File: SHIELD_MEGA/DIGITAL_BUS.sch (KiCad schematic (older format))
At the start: 38 parts

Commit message: Finished digital sheet
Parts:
- removed J?: Conn_01x03_Male, symbol Connector:Conn_01x03_Male
- added J?: Conn_01x03_Male, symbol Connector:Conn_01x03_Male
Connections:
- net 5V: now also J?.2 (Pin_2)
- net DGND: now also J?.3 (Pin_3)
- net D12: now reaches J?.1 (Pin_1)
- net D13: now reaches J?.1 (Pin_1)
- net D22: now reaches J?.1 (Pin_1)
- net D23: now reaches J?.1 (Pin_1)
- net D24: now reaches J?.1 (Pin_1)
- net D25: now reaches J?.1 (Pin_1)
- net D26: now reaches J?.1 (Pin_1)
- net D28: now reaches J?.1 (Pin_1)
- net D29: now reaches J?.1 (Pin_1)
- net D30: now reaches J?.1 (Pin_1)
- net D31: now reaches J?.1 (Pin_1)
- net D32: now reaches J?.1 (Pin_1)
- net D33: now reaches J?.1 (Pin_1)
- net D34: now reaches J?.1 (Pin_1)
- net D35: now reaches J?.1 (Pin_1)
- net D36: now reaches J?.1 (Pin_1)
- net D37: now reaches J?.1 (Pin_1)
- net D38: now reaches J?.1 (Pin_1)
- net D39: now reaches J?.1 (Pin_1)
- net D40: now reaches J?.1 (Pin_1)
- net D41: now reaches J?.1 (Pin_1)
- net D42: now reaches J?.1 (Pin_1)
- net D43: now reaches J?.1 (Pin_1)
- net D44: now reaches J?.1 (Pin_1)
- net D45: now reaches J?.1 (Pin_1)
- net D46: now reaches J?.1 (Pin_1)
- net D47: now reaches J?.1 (Pin_1)
- net D48: now reaches J?.1 (Pin_1)
- net D49: now reaches J?.1 (Pin_1)
- net D2_INTO0: now reaches J?.1 (Pin_1)
- net D3_INT1: now reaches J?.1 (Pin_1)
- net D4_PWM: now reaches J?.1 (Pin_1)
- net D5_PWM: now reaches J?.1 (Pin_1)
- net D6_PWM: now reaches J?.1 (Pin_1)
- net D7_PWM: now reaches J?.1 (Pin_1)
- net D8: now reaches J?.1 (Pin_1)
- net D9: now reaches J?.1 (Pin_1)
- new net D27: J?.1 (Pin_1)
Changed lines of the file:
@@
-$Comp
-L Connector:Conn_01x03_Male J?
-U 1 1 61D7858B
-P 2950 1100
-F 0 "J?" H 3058 1381 50  0000 C CNN
-F 1 "Conn_01x03_Male" H 3058 1290 50  0000 C CNN
-F 2 "" H 2950 1100 50  0001 C CNN
-F 3 "~" H 2950 1100 50  0001 C CNN
-	1    2950 1100
-	1    0    0    -1
-$EndComp
-Wire Wire Line
-	3150 1200 3550 1200
-Text HLabel 3550 1200 2    50   Input ~ 0
-DGND
-Text HLabel 3550 1100 2    50   Input ~ 0
-5V
-Wire Wire Line
-	3550 1100 3150 1100
 $Comp
 L Connector:Conn_01x03_Male J?
@@
 Wire Wire Line
 	9550 5150 9150 5150
+Wire Wire Line
+	1650 1000 2050 1000
+$Comp
+L Connector:Conn_01x03_Male J?
+U 1 1 61DC449F
+P 2950 1100
+F 0 "J?" H 3058 1381 50  0000 C CNN
+F 1 "Conn_01x03_Male" H 3058 1290 50  0000 C CNN
+F 2 "" H 2950 1100 50  0001 C CNN
+F 3 "~" H 2950 1100 50  0001 C CNN
+	1    2950 1100
+	1    0    0    -1
+$EndComp
+Wire Wire Line
+	3150 1200 3550 1200
+Text HLabel 3550 1200 2    50   Input ~ 0
+DGND
+Text HLabel 3550 1100 2    50   Input ~ 0
+5V
+Wire Wire Line
+	3550 1100 3150 1100
+Wire Wire Line
+	3150 1000 3550 1000
+Wire Wire Line
+	1650 2000 2050 2000
+Wire Wire Line
+	3150 2000 3550 2000
+Wire Wire Line
+	4650 1000 5050 1000
+Wire Wire Line
+	4650 2000 5050 2000
+Wire Wire Line
+	1650 3000 2050 3000
+Wire Wire Line
+	3150 3000 3550 3000
+Wire Wire Line
+	4650 3000 5050 3000
+Wire Wire Line
+	6150 3000 6550 3000
+Wire Wire Line
+	6150 2000 6550 2000
+Wire Wire Line
+	6150 1000 6550 1000
+Wire Wire Line
+	1650 4000 2050 4000
+Wire Wire Line
+	3150 4000 3550 4000
+Wire Wire Line
+	4650 4000 5050 4000
+Wire Wire Line
+	6150 4000 6550 4000
+Wire Wire Line
+	7650 4000 8050 4000
+Wire Wire Line
+	7650 3000 8050 3000
+Wire Wire Line
+	7650 5050 8050 5050
+Wire Wire Line
+	6150 5050 6550 5050
+Wire Wire Line
+	4650 5050 5050 5050
+Wire Wire Line
+	3150 5050 3550 5050
+Wire Wire Line
+	1650 5050 2050 5050
+Wire Wire Line
+	1650 6050 2050 6050
+Wire Wire Line
+	1650 7050 2050 7050
+Wire Wire Line
+	3150 7050 3550 7050
+Wire Wire Line
+	4650 7050 5050 7050
+Wire Wire Line
+	6150 7050 6550 7050
+Wire Wire Line
+	6150 6050 6550 6050
+Wire Wire Line
+	9150 5050 9550 5050
+Wire Wire Line
+	9150 4000 9550 4000
+Wire Wire Line
+	9150 3000 9550 3000
+Wire Wire Line
+	9150 2000 9550 2000
+Wire Wire Line
+	7650 2000 8050 2000
+Wire Wire Line
+	7650 1000 8050 1000
+Wire Wire Line
+	9150 1000 9550 1000
+Wire Wire Line
+	3150 6050 3550 6050
+Wire Wire Line
+	4650 6050 5050 6050
+Text HLabel 2050 1000 2    50   Input ~ 0
+D12
+Text HLabel 2050 2000 2    50   Input ~ 0
+D13
+Text HLabel 2050 3000 2    50   Input ~ 0
+D22
+Text HLabel 2050 4000 2    50   Input ~ 0
+D23
+Text HLabel 2050 5050 2    50   Input ~ 0
+D24
+Text HLabel 2050 6050 2    50   Input ~ 0
+D25
+Text HLabel 2050 7050 2    50   Input ~ 0
+D26
+Text HLabel 3550 1000 2    50   Input ~ 0
+D27
+Text HLabel 3550 2000 2    50   Input ~ 0
+D28
+Text HLabel 3550 3000 2    50   Input ~ 0
+D29
+Text HLabel 3550 4000 2    50   Input ~ 0
+D30
+Text HLabel 3550 5050 2    50   Input ~ 0
+D31
+Text HLabel 3550 7050 2    50   Input ~ 0
+D33
+Text HLabel 3550 6050 2    50   Input ~ 0
+D32
+Text HLabel 5050 1000 2    50   Input ~ 0
+D34
+Text HLabel 5050 2000 2    50   Input ~ 0
+D35
+Text HLabel 5050 3000 2    50   Input ~ 0
+D36
+Text HLabel 5050 4000 2    50   Input ~ 0
+D37
+Text HLabel 5050 5050 2    50   Input ~ 0
+D38
+Text HLabel 5050 6050 2    50   Input ~ 0
+D39
+Text HLabel 5050 7050 2    50   Input ~ 0
+D40
+Text HLabel 6550 1000 2    50   Input ~ 0
+D41
+Text HLabel 6550 2000 2    50   Input ~ 0
+D42
+Text HLabel 6550 3000 2    50   Input ~ 0
+D43
+Text HLabel 6550 4000 2    50   Input ~ 0
+D44
+Text HLabel 6550 5050 2    50   Input ~ 0
+D45
+Text HLabel 6550 6050 2    50   Input ~ 0
+D46
+Text HLabel 6550 7050 2    50   Input ~ 0
+D47
+Text HLabel 8050 1000 2    50   Input ~ 0
+D48
+Text HLabel 8050 2000 2    50   Input ~ 0
+D49
+Text HLabel 8050 3000 2    50   Input ~ 0
+D2_INTO0
+Text HLabel 8050 4000 2    50   Input ~ 0
+D3_INT1
+Text HLabel 8050 5050 2    50   Input ~ 0
+D4_PWM
+Text HLabel 9550 1000 2    50   Input ~ 0
+D5_PWM
+Text HLabel 9550 2000 2    50   Input ~ 0
+D6_PWM
+Text HLabel 9550 3000 2    50   Input ~ 0
+D7_PWM
+Text HLabel 9550 4000 2    50   Input ~ 0
+D8
+Text HLabel 9550 5050 2    50   Input ~ 0
+D9
 $EndSCHEMATC

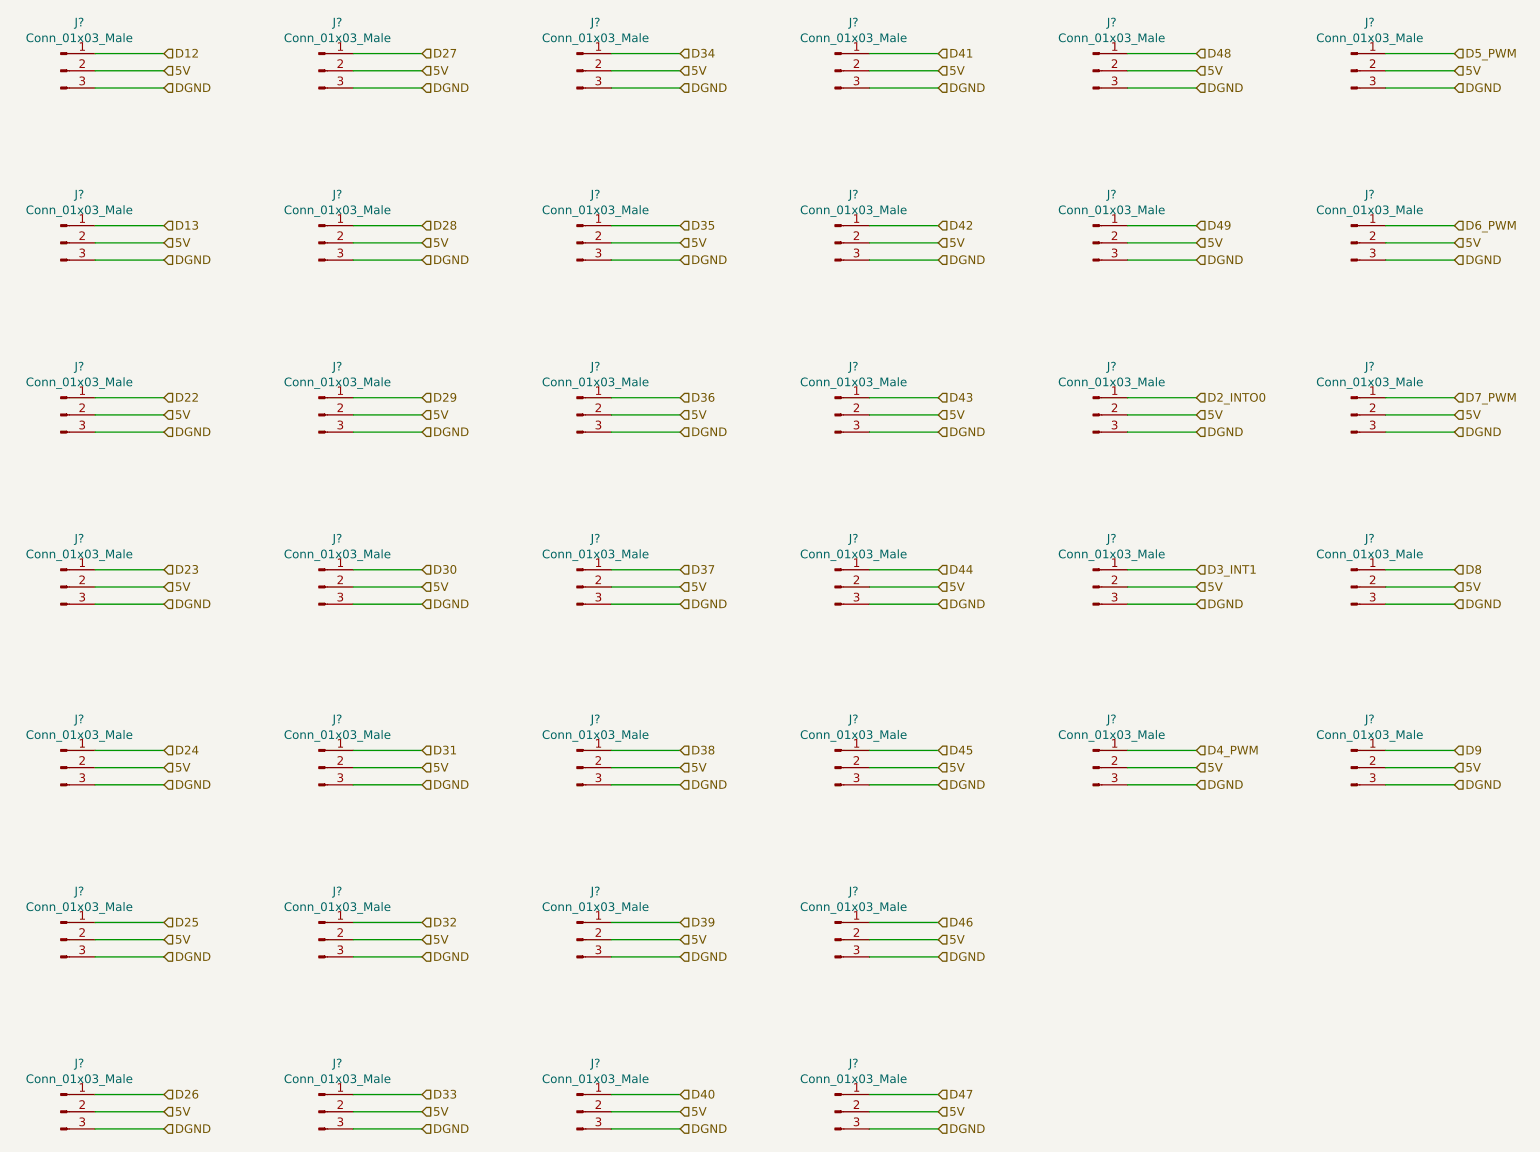
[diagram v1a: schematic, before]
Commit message: Anotations of ref. parts in digital sheet
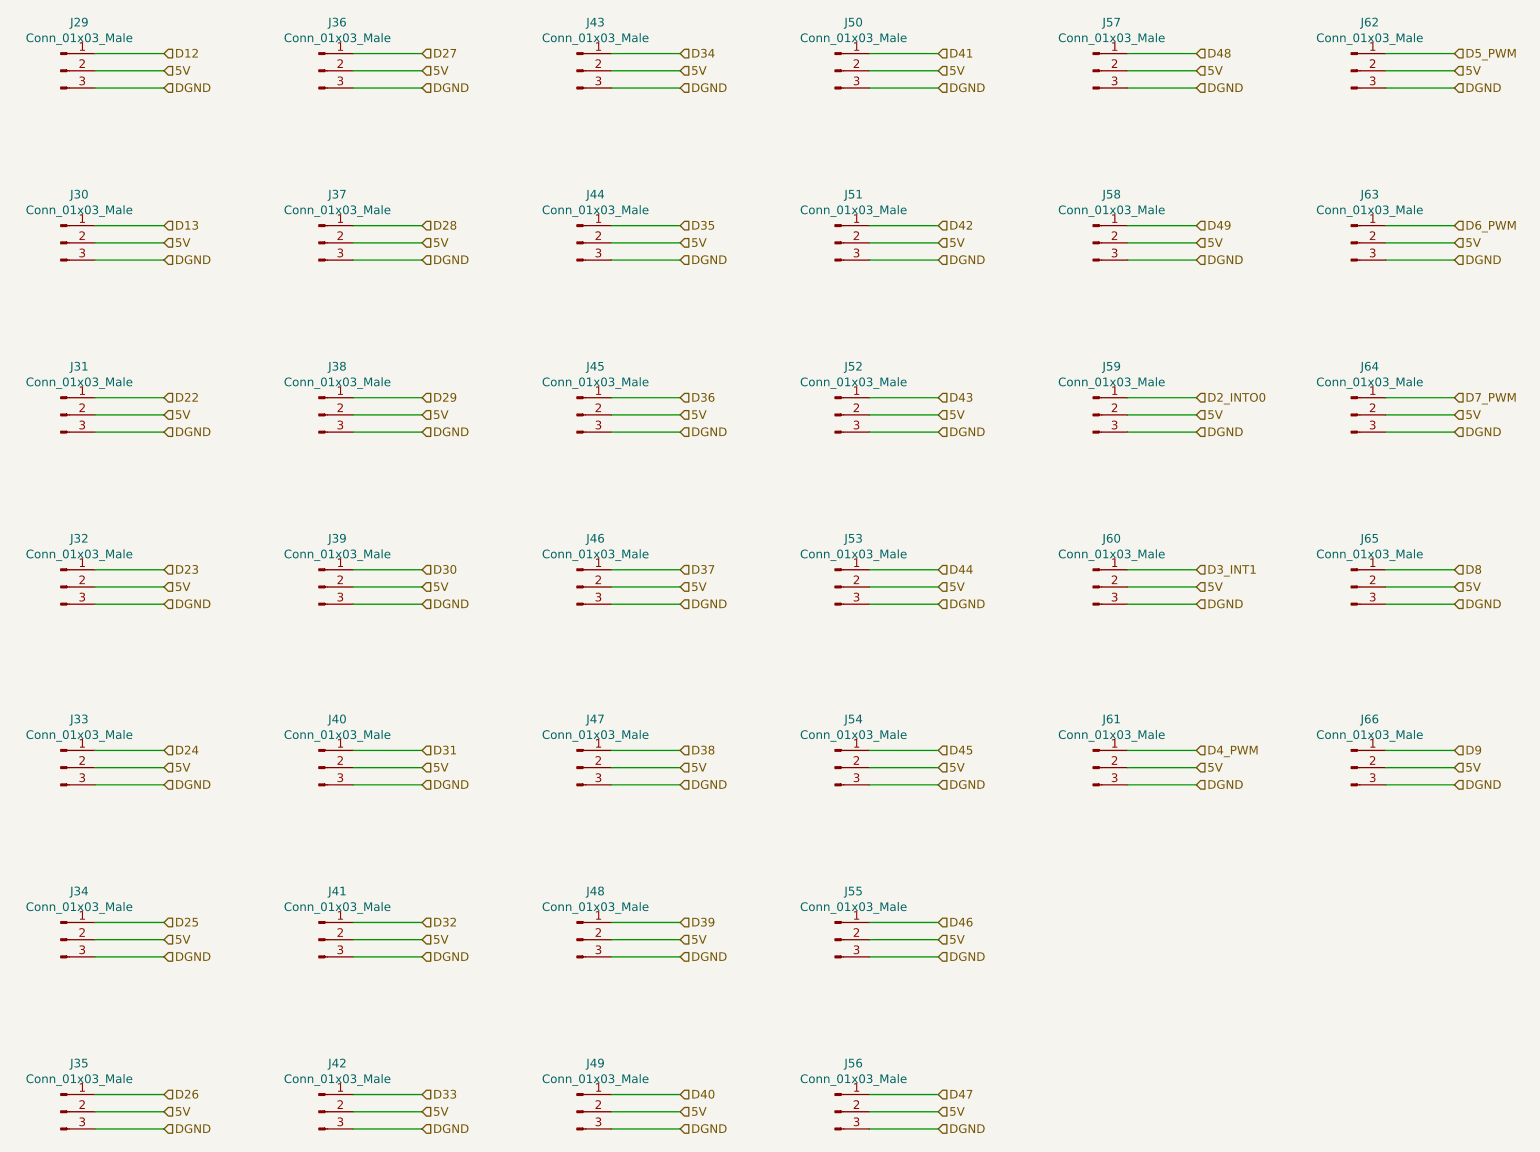
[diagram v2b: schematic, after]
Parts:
- gave numbers to parts that had none: 38

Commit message: Linking symbols with footprints in digital sheet
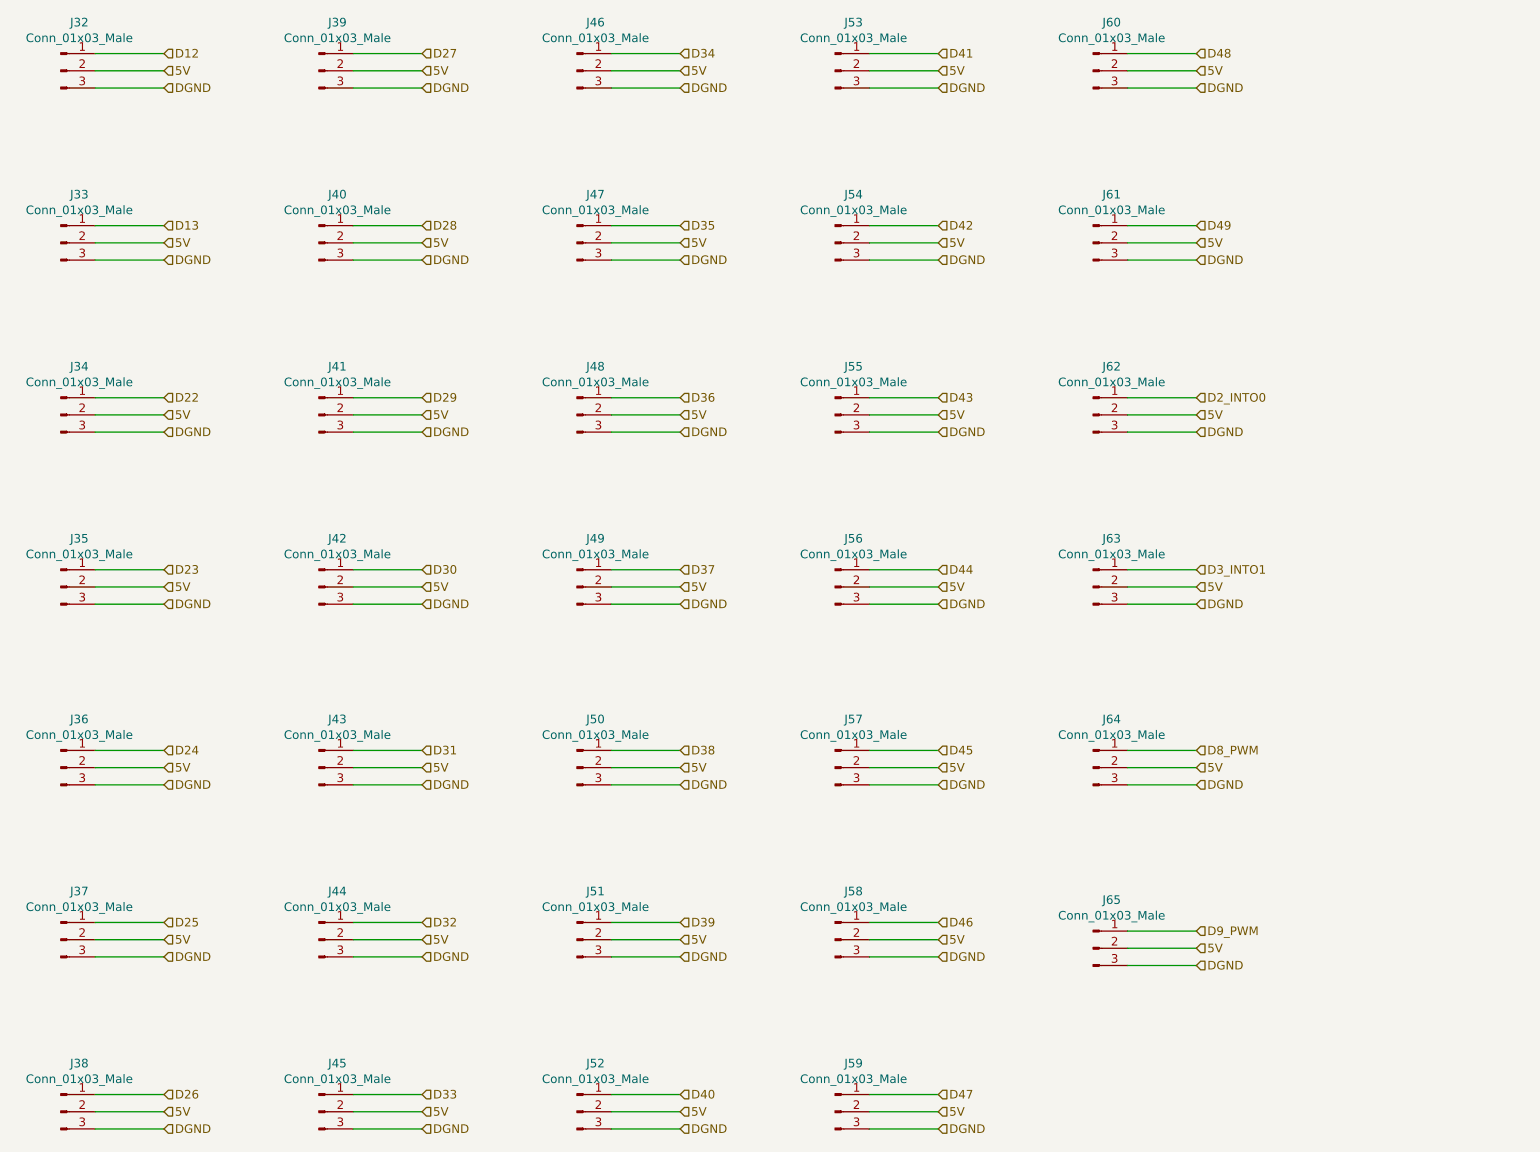
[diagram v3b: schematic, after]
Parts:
- removed J61, J62, J63, J64: Conn_01x03_Male, symbol Connector:Conn_01x03_Male
- J32: renamed from J29; footprint (none) -> Connector_PinHeader_2.54mm:PinHeader_1x03_P2.54mm_Vertical
- J33: renamed from J30; footprint (none) -> Connector_PinHeader_2.54mm:PinHeader_1x03_P2.54mm_Vertical
- J34: renamed from J31; footprint (none) -> Connector_PinHeader_2.54mm:PinHeader_1x03_P2.54mm_Vertical
- J35: renamed from J32; footprint (none) -> Connector_PinHeader_2.54mm:PinHeader_1x03_P2.54mm_Vertical
- J36: renamed from J33; footprint (none) -> Connector_PinHeader_2.54mm:PinHeader_1x03_P2.54mm_Vertical
- J37: renamed from J34; footprint (none) -> Connector_PinHeader_2.54mm:PinHeader_1x03_P2.54mm_Vertical
- J38: renamed from J35; footprint (none) -> Connector_PinHeader_2.54mm:PinHeader_1x03_P2.54mm_Vertical
- J39: renamed from J36; footprint (none) -> Connector_PinHeader_2.54mm:PinHeader_1x03_P2.54mm_Vertical
- J40: renamed from J37; footprint (none) -> Connector_PinHeader_2.54mm:PinHeader_1x03_P2.54mm_Vertical
- J41: renamed from J38; footprint (none) -> Connector_PinHeader_2.54mm:PinHeader_1x03_P2.54mm_Vertical
- J42: renamed from J39; footprint (none) -> Connector_PinHeader_2.54mm:PinHeader_1x03_P2.54mm_Vertical
- J43: renamed from J40; footprint (none) -> Connector_PinHeader_2.54mm:PinHeader_1x03_P2.54mm_Vertical
- J44: renamed from J41; footprint (none) -> Connector_PinHeader_2.54mm:PinHeader_1x03_P2.54mm_Vertical
- J45: renamed from J42; footprint (none) -> Connector_PinHeader_2.54mm:PinHeader_1x03_P2.54mm_Vertical
- J46: renamed from J43; footprint (none) -> Connector_PinHeader_2.54mm:PinHeader_1x03_P2.54mm_Vertical
- J47: renamed from J44; footprint (none) -> Connector_PinHeader_2.54mm:PinHeader_1x03_P2.54mm_Vertical
- J48: renamed from J45; footprint (none) -> Connector_PinHeader_2.54mm:PinHeader_1x03_P2.54mm_Vertical
- J49: renamed from J46; footprint (none) -> Connector_PinHeader_2.54mm:PinHeader_1x03_P2.54mm_Vertical
- J50: renamed from J47; footprint (none) -> Connector_PinHeader_2.54mm:PinHeader_1x03_P2.54mm_Vertical
- J51: renamed from J48; footprint (none) -> Connector_PinHeader_2.54mm:PinHeader_1x03_P2.54mm_Vertical
- J52: renamed from J49; footprint (none) -> Connector_PinHeader_2.54mm:PinHeader_1x03_P2.54mm_Vertical
- J53: renamed from J50; footprint (none) -> Connector_PinHeader_2.54mm:PinHeader_1x03_P2.54mm_Vertical
- J54: renamed from J51; footprint (none) -> Connector_PinHeader_2.54mm:PinHeader_1x03_P2.54mm_Vertical
- J55: renamed from J52; footprint (none) -> Connector_PinHeader_2.54mm:PinHeader_1x03_P2.54mm_Vertical
- J56: renamed from J53; footprint (none) -> Connector_PinHeader_2.54mm:PinHeader_1x03_P2.54mm_Vertical
- J57: renamed from J54; footprint (none) -> Connector_PinHeader_2.54mm:PinHeader_1x03_P2.54mm_Vertical
- J58: renamed from J55; footprint (none) -> Connector_PinHeader_2.54mm:PinHeader_1x03_P2.54mm_Vertical
- J59: renamed from J56; footprint (none) -> Connector_PinHeader_2.54mm:PinHeader_1x03_P2.54mm_Vertical
- J60: renamed from J57; footprint (none) -> Connector_PinHeader_2.54mm:PinHeader_1x03_P2.54mm_Vertical
- J61: renamed from J58; footprint (none) -> Connector_PinHeader_2.54mm:PinHeader_1x03_P2.54mm_Vertical
- J62: renamed from J59; footprint (none) -> Connector_PinHeader_2.54mm:PinHeader_1x03_P2.54mm_Vertical
- J63: renamed from J60; footprint (none) -> Connector_PinHeader_2.54mm:PinHeader_1x03_P2.54mm_Vertical
- J64: renamed from J65; footprint (none) -> Connector_PinHeader_2.54mm:PinHeader_1x03_P2.54mm_Vertical
- J65: renamed from J66; footprint (none) -> Connector_PinHeader_2.54mm:PinHeader_1x03_P2.54mm_Vertical
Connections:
- net D3_INT1 renamed D3_INTO1
- net D8 renamed D8_PWM
- net D9 renamed D9_PWM
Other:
- moved on the sheet: J64, J65
